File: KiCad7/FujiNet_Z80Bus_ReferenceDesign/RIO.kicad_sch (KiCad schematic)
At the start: 6 parts

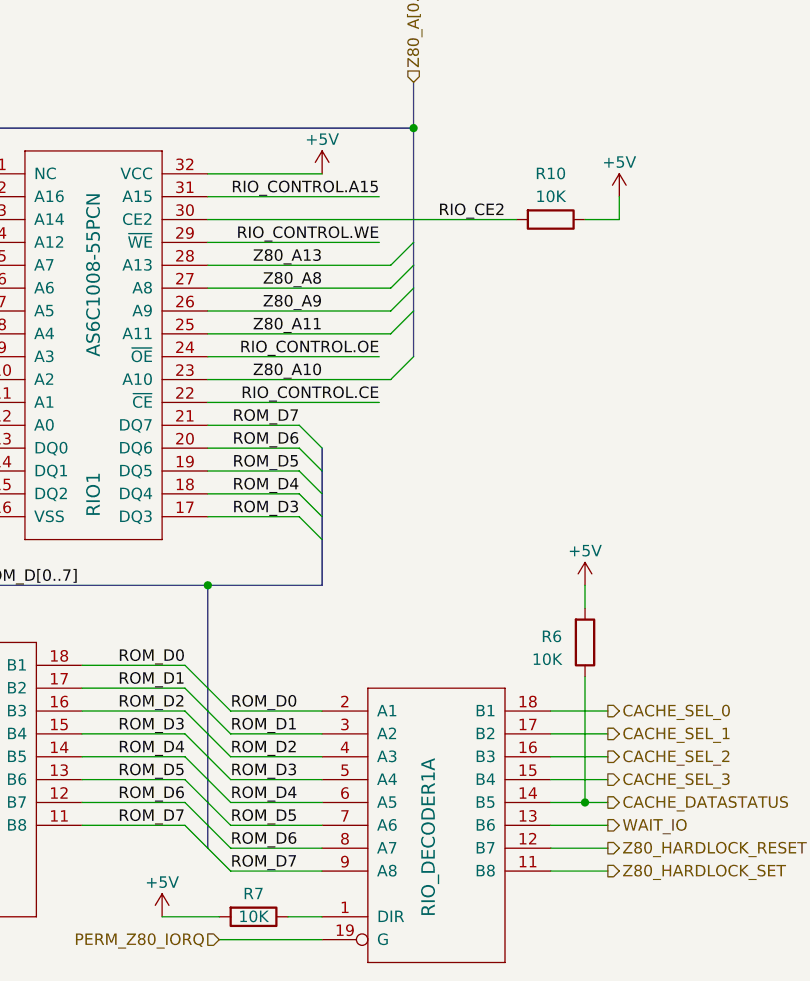
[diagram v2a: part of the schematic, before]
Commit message: Unpicked CoreLogic Buses, some symbol updates
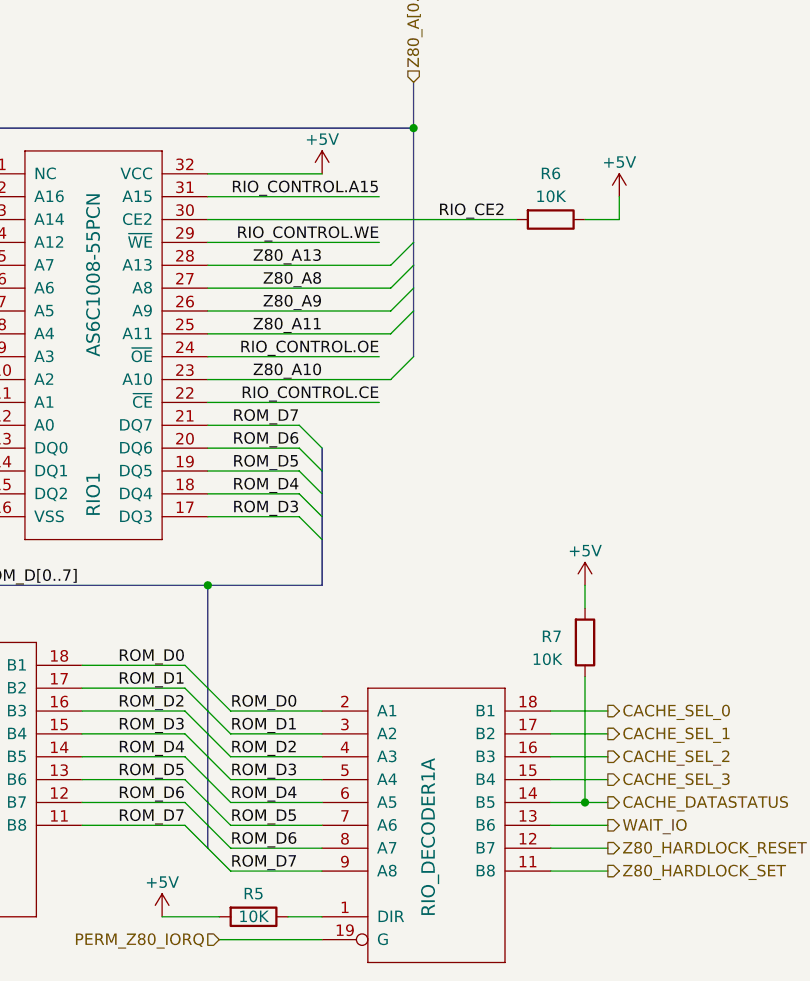
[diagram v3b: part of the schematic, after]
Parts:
- renumbered R7 to R5, R10 to R6, R6 to R7
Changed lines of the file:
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@@
   (symbol (lib_id "Device:R") (at 160.02 52.07 270) (unit 1)
     (in_bom yes) (on_board yes) (dnp no) (fields_autoplaced)
-    (property "Reference" "R10" (at 160.02 46.99 90)
+    (property "Reference" "R6" (at 160.02 46.99 90)
       (effects (font (size 1.27 1.27)))
     )
@@
       (project "FujiNet_Z80Bus_ReferenceDesign"
         (path "/532c0392-800e-45cc-8170-6d32f2390e83/00000000-0000-0000-0000-0000ad721c5e"
-          (reference "R10") (unit 1)
+          (reference "R6") (unit 1)
         )
       )
@@
   (symbol (lib_id "power:GND") (at 91.44 85.09 0) (unit 1)
     (in_bom yes) (on_board yes) (dnp no)
-    (property "Reference" "#PWR023" (at 91.44 91.44 0)
+    (property "Reference" "#PWR019" (at 91.44 91.44 0)
       (effects (font (size 1.27 1.27)) hide)
     )
@@
       (project "FujiNet_Z80Bus_ReferenceDesign"
         (path "/532c0392-800e-45cc-8170-6d32f2390e83/00000000-0000-0000-0000-0000ad721c5e"
-          (reference "#PWR023") (unit 1)
+          (reference "#PWR019") (unit 1)
         )
       )
@@
   (symbol (lib_id "Device:R") (at 127 129.54 270) (unit 1)
     (in_bom yes) (on_board yes) (dnp no) (fields_autoplaced)
-    (property "Reference" "R7" (at 127 127 90)
+    (property "Reference" "R5" (at 127 127 90)
       (effects (font (size 1.27 1.27)))
     )
@@
       (project "FujiNet_Z80Bus_ReferenceDesign"
         (path "/532c0392-800e-45cc-8170-6d32f2390e83/00000000-0000-0000-0000-0000ad721c5e"
-          (reference "R7") (unit 1)
+          (reference "R5") (unit 1)
         )
         (path "/532c0392-800e-45cc-8170-6d32f2390e83/00000000-0000-0000-0000-0000ae2cbb6b"
@@
   (symbol (lib_id "power:+5V") (at 116.84 129.54 0) (unit 1)
     (in_bom yes) (on_board yes) (dnp no) (fields_autoplaced)
-    (property "Reference" "#PWR024" (at 116.84 133.35 0)
+    (property "Reference" "#PWR020" (at 116.84 133.35 0)
       (effects (font (size 1.27 1.27)) hide)
     )
@@
       (project "FujiNet_Z80Bus_ReferenceDesign"
         (path "/532c0392-800e-45cc-8170-6d32f2390e83/00000000-0000-0000-0000-0000ad721c5e"
-          (reference "#PWR024") (unit 1)
+          (reference "#PWR020") (unit 1)
         )
       )
@@
   (symbol (lib_id "power:+5V") (at 134.62 46.99 0) (unit 1)
     (in_bom yes) (on_board yes) (dnp no) (fields_autoplaced)
-    (property "Reference" "#PWR026" (at 134.62 50.8 0)
+    (property "Reference" "#PWR021" (at 134.62 50.8 0)
       (effects (font (size 1.27 1.27)) hide)
     )
@@
       (project "FujiNet_Z80Bus_ReferenceDesign"
         (path "/532c0392-800e-45cc-8170-6d32f2390e83/00000000-0000-0000-0000-0000ad721c5e"
-          (reference "#PWR026") (unit 1)
+          (reference "#PWR021") (unit 1)
         )
       )
@@
   (symbol (lib_id "power:+5V") (at 167.64 49.53 0) (unit 1)
     (in_bom yes) (on_board yes) (dnp no) (fields_autoplaced)
-    (property "Reference" "#PWR028" (at 167.64 53.34 0)
+    (property "Reference" "#PWR023" (at 167.64 53.34 0)
       (effects (font (size 1.27 1.27)) hide)
     )
@@
       (project "FujiNet_Z80Bus_ReferenceDesign"
         (path "/532c0392-800e-45cc-8170-6d32f2390e83/00000000-0000-0000-0000-0000ad721c5e"
-          (reference "#PWR028") (unit 1)
+          (reference "#PWR023") (unit 1)
         )
       )
@@
   (symbol (lib_id "Device:R") (at 163.83 99.06 0) (mirror x) (unit 1)
     (in_bom yes) (on_board yes) (dnp no) (fields_autoplaced)
-    (property "Reference" "R6" (at 161.29 98.425 0)
+    (property "Reference" "R7" (at 161.29 98.425 0)
       (effects (font (size 1.27 1.27)) (justify right))
     )
@@
       (project "FujiNet_Z80Bus_ReferenceDesign"
         (path "/532c0392-800e-45cc-8170-6d32f2390e83/00000000-0000-0000-0000-0000ad721c5e"
-          (reference "R6") (unit 1)
+          (reference "R7") (unit 1)
         )
         (path "/532c0392-800e-45cc-8170-6d32f2390e83/00000000-0000-0000-0000-0000ae2cbb6b"
@@
   (symbol (lib_id "power:+5V") (at 163.83 92.71 0) (unit 1)
     (in_bom yes) (on_board yes) (dnp no) (fields_autoplaced)
-    (property "Reference" "#PWR025" (at 163.83 96.52 0)
+    (property "Reference" "#PWR022" (at 163.83 96.52 0)
       (effects (font (size 1.27 1.27)) hide)
     )
@@
       (project "FujiNet_Z80Bus_ReferenceDesign"
         (path "/532c0392-800e-45cc-8170-6d32f2390e83/00000000-0000-0000-0000-0000ad721c5e"
-          (reference "#PWR025") (unit 1)
+          (reference "#PWR022") (unit 1)
         )
         (path "/532c0392-800e-45cc-8170-6d32f2390e83/6a1fd481-1635-4a64-b244-c204161ad407"

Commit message: KiCad - ALMOST ERROR FREE!!!!
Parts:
- RIO_DECODER1, Z80-RIO_DATA1: symbol FujiNet_Z80Bus_Reference-rescue:74245N-Z80Decoder-eagle-import -> 74xx:74HC245
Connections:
- net +5V: now also RIO_DECODER1.20 (VCC), Z80-RIO_DATA1.20 (VCC)
- net GND: now also RIO_DECODER1.10 (GND), Z80-RIO_DATA1.10 (GND)
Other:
- moved on the sheet: R5, R7

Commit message: KiCad - Library fixes and AS6C1008 memory added
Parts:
- added U?: AS6C1008-55PCN, Package_DIP:DIP-32_W15.24mm, symbol Memory_RAM:AS6C4008-55PCN
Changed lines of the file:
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@@
+    )
+  )
+  (symbol (lib_id "Memory_RAM:AS6C4008-55PCN") (at 187.96 50.8 0) (unit 1)
+    (in_bom yes) (on_board yes) (dnp no) (fields_autoplaced)
+    (property "Reference" "U?" (at 189.9159 21.59 0)
+      (effects (font (size 1.27 1.27)) (justify left))
+    )
+    (property "Value" "AS6C1008-55PCN" (at 189.9159 24.13 0)
+      (effects (font (size 1.27 1.27)) (justify left))
+    )
+    (property "Footprint" "Package_DIP:DIP-32_W15.24mm" (at 187.96 48.26 0)
+      (effects (font (size 1.27 1.27)) hide)
+    )
+    (property "Datasheet" "https://www.alliancememory.com/wp-content/uploads/pdf/AS6C1008.pdf" (at 187.96 48.26 0)
+      (effects (font (size 1.27 1.27)) hide)
+    )
+    (pin "16")
+    (pin "32")
+    (pin "1")
+    (pin "10")
+    (pin "11")
+    (pin "12")
+    (pin "13")
+    (pin "14")
+    (pin "15")
+    (pin "17")
+    (pin "18")
+    (pin "19")
+    (pin "2")
+    (pin "20")
+    (pin "21")
+    (pin "22")
+    (pin "23")
+    (pin "24")
+    (pin "25")
+    (pin "26")
+    (pin "27")
+    (pin "28")
+    (pin "29")
+    (pin "3")
+    (pin "30")
+    (pin "31")
+    (pin "4")
+    (pin "5")
+    (pin "6")
+    (pin "7")
+    (pin "8")
+    (pin "9")
+    (instances
+      (project "FujiNet_Z80Bus_ReferenceDesign"
+        (path "/532c0392-800e-45cc-8170-6d32f2390e83/00000000-0000-0000-0000-0000ad721c5e"
+          (reference "U?") (unit 1)
+        )
+      )
     )
   )

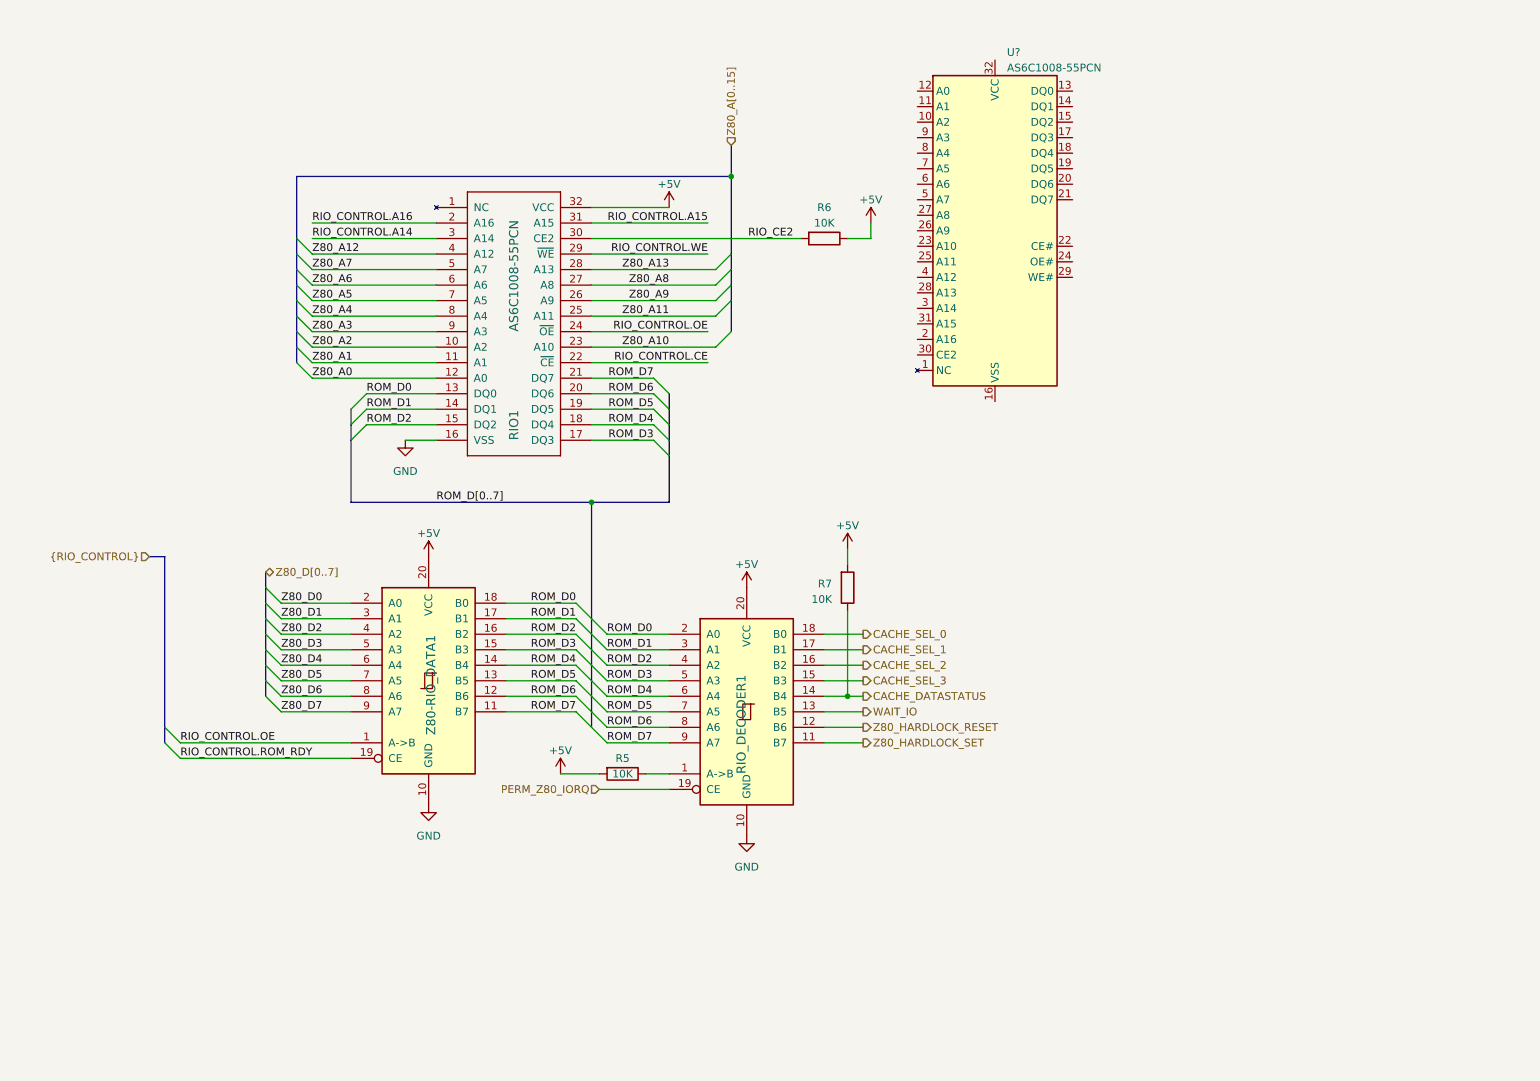
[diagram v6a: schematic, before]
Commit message: KiCad - Swapped out RIO and CACHE symbols
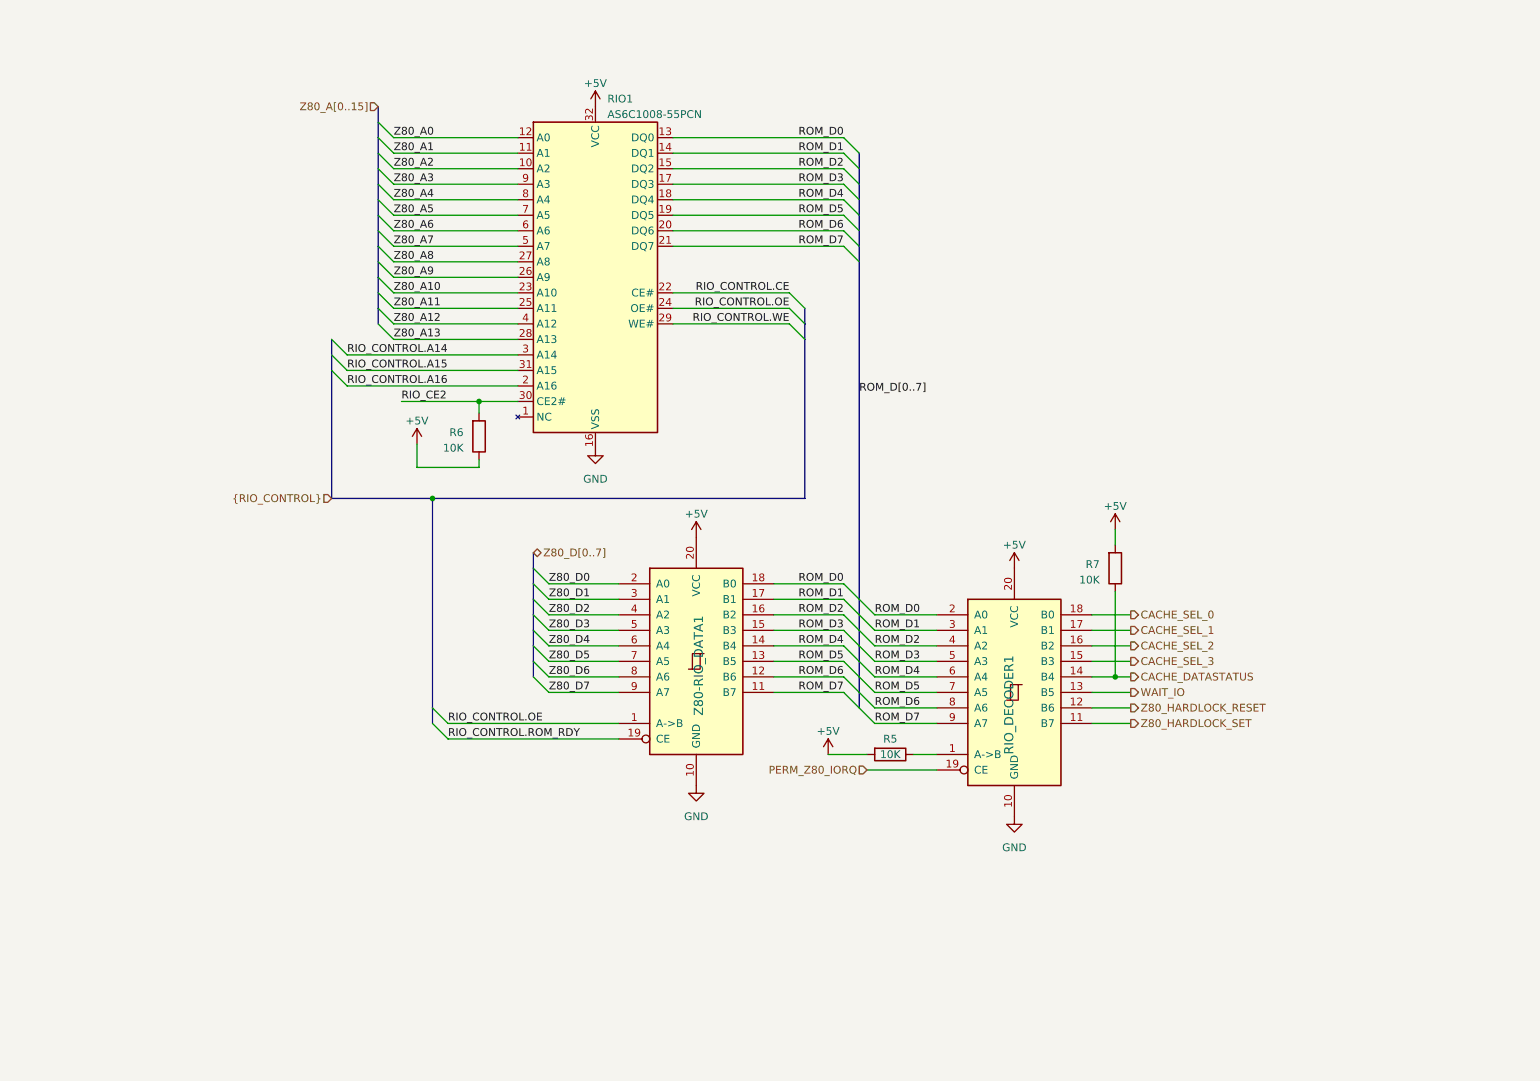
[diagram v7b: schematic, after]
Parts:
- removed RIO1: AS6C1008-55PCN, Package_DIP:DIP-32_W15.24mm_Socket, symbol FujiNet_Z80Bus_Reference-rescue:AS6C1008-55PCN-Z80Decoder-eagle-import
- RIO1: renamed from U?; symbol Memory_RAM:AS6C4008-55PCN -> FujiNet_Memory_RAM:AS6C1008-55PCN
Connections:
- net +5V: now also RIO1.32 (VCC)
- net GND: now also RIO1.16 (VSS)
- net RIO_CE2: now also RIO1.30 (CE2#)
- net RIO_CONTROL.A14: now also RIO1.3 (A14)
- net RIO_CONTROL.A15: now also RIO1.31 (A15)
- net RIO_CONTROL.A16: now also RIO1.2 (A16)
- net RIO_CONTROL.CE: now also RIO1.22 (CE#)
- net RIO_CONTROL.OE: now also RIO1.24 (OE#)
- net RIO_CONTROL.WE: now also RIO1.29 (WE#)
- net ROM_D0: now also RIO1.13 (DQ0)
- net ROM_D1: now also RIO1.14 (DQ1)
- net ROM_D2: now also RIO1.15 (DQ2)
- net ROM_D3: now also RIO1.17 (DQ3)
- net ROM_D4: now also RIO1.18 (DQ4)
- net ROM_D5: now also RIO1.19 (DQ5)
- net ROM_D6: now also RIO1.20 (DQ6)
- net ROM_D7: now also RIO1.21 (DQ7)
- net Z80_A0: now also RIO1.12 (A0)
- net Z80_A1: now also RIO1.11 (A1)
- net Z80_A10: now also RIO1.23 (A10)
- net Z80_A11: now also RIO1.25 (A11)
- net Z80_A12: now also RIO1.4 (A12)
- net Z80_A13: now also RIO1.28 (A13)
- net Z80_A2: now also RIO1.10 (A2)
- net Z80_A3: now also RIO1.9 (A3)
- net Z80_A4: now also RIO1.8 (A4)
- net Z80_A5: now also RIO1.7 (A5)
- net Z80_A6: now also RIO1.6 (A6)
- net Z80_A7: now also RIO1.5 (A7)
- net Z80_A8: now also RIO1.27 (A8)
- net Z80_A9: now also RIO1.26 (A9)
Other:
- moved on the sheet: R5, R6, R7, RIO1, RIO_DECODER1, Z80-RIO_DATA1

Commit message: KiCAD PCB layout testing
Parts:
- RIO_DECODER1, Z80-RIO_DATA1: value 74245N -> 74HC245N
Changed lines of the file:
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@@
       (effects (font (size 1.4986 1.4986)) (justify left bottom))
     )
-    (property "Value" "74245N" (at 183.515 144.145 0)
+    (property "Value" "74HC245N" (at 183.515 144.145 0)
       (effects (font (size 1.4986 1.4986)) (justify left bottom) hide)
     )
@@
       (effects (font (size 1.4986 1.4986)) (justify left bottom))
     )
-    (property "Value" "74245N" (at 131.445 139.065 0)
+    (property "Value" "74HC245N" (at 131.445 139.065 0)
       (effects (font (size 1.4986 1.4986)) (justify left bottom) hide)
     )
